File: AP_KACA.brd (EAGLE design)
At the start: 47 x 29 mm, 50 parts, among them IC1 MCP1252-33X50, J1 FTDI_DEVICE, M1 WIRELESS-NRF24L01, Q1 BSS123, Q2 BSS123, Q3 BSS123, Q4 BSS123, U1 ATMEGA328P_TQFP, U3 GY-521MPU6050, Y1 8MHz

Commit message: Airwires gone
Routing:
- net MOTOR_3: track 1.77 -> 41.8 mm, vias 1 -> 2
- net AGND: track 7.90 -> 47.0 mm, vias 1 -> 4
- net V_READER: track 2.09 -> 22.8 mm, vias 0 -> 3
- net MGND: track 0.00 -> 20.3 mm, vias 0 -> 1
- net SDA: track 0.00 -> 17.3 mm, vias 0 -> 2
- net DGND: track 52.4 -> 56.3 mm
- net GND: track 0.00 -> 1.32 mm
- net N$9: track 4.49 -> 5.57 mm

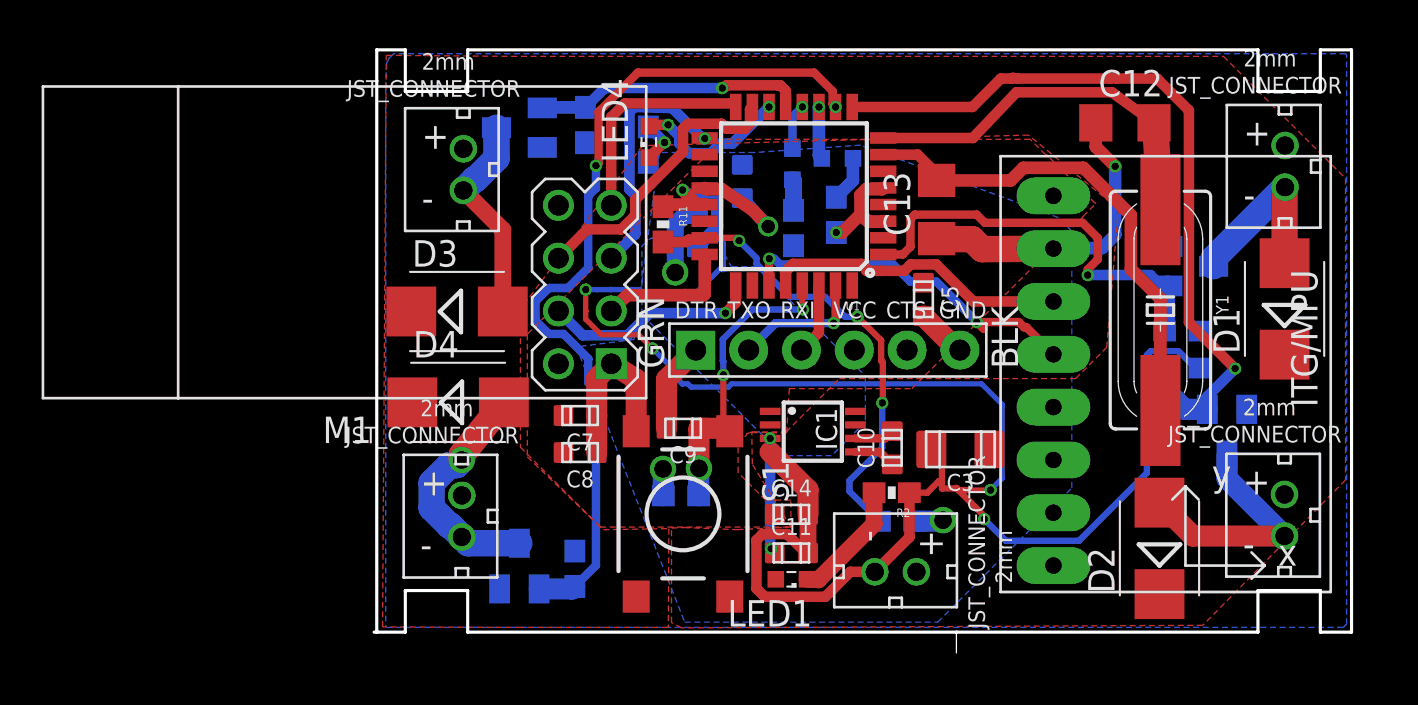
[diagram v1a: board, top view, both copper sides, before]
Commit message: finished first draft of board
got rid of all the drc errors
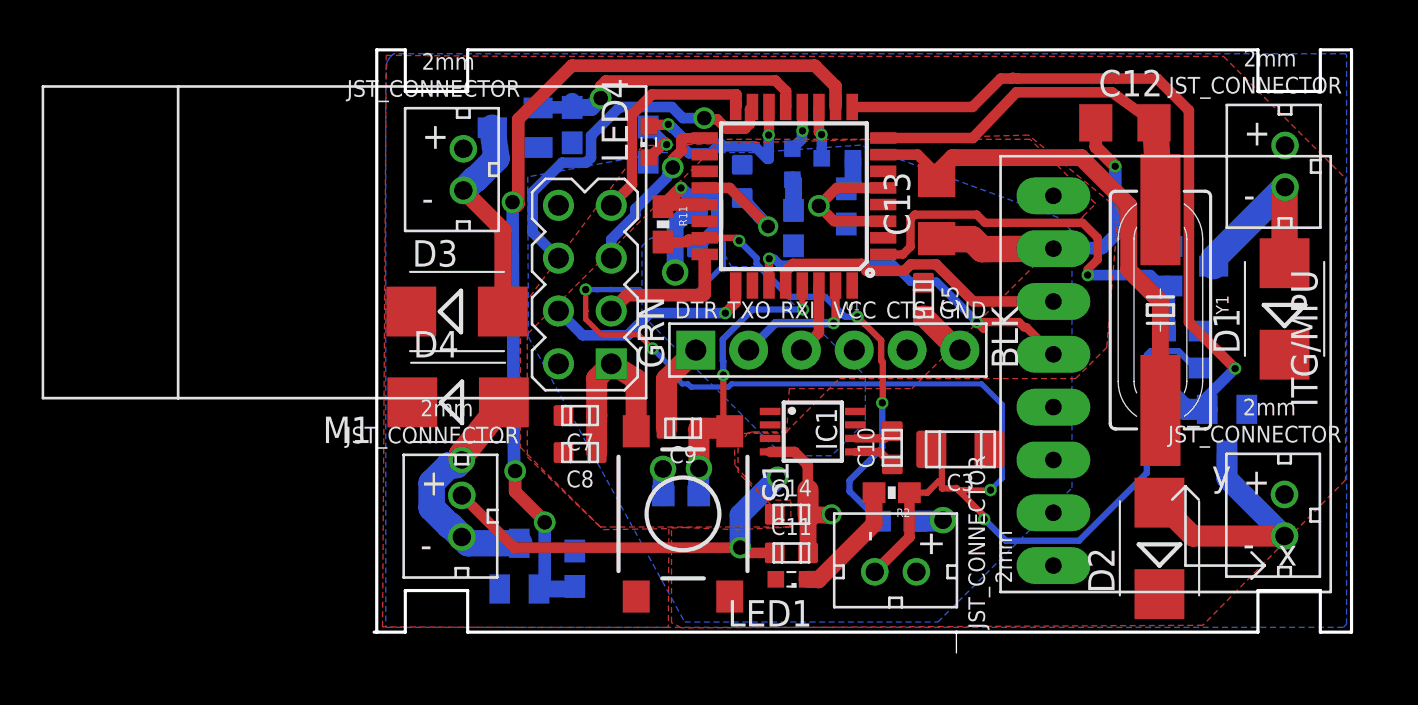
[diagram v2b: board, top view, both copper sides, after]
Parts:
- moved R5 0.63 mm to (9.53, 24.4)
- moved R7 0.63 mm to (22.7, 20.5)
- moved Q3 0.20 mm to (6.78, 24.3)
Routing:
- net 3.7V: track 7.29 -> 22.0 mm
- net DGND: track 56.3 -> 48.4 mm, vias 2 -> 3
- net MOSI: track 14.0 -> 17.9 mm, vias 0 -> 1
- net SCK: track 12.0 -> 8.25 mm
- net LED_3: track 7.51 -> 9.65 mm
- net MOTOR_3: track 41.8 -> 43.3 mm, vias 2 -> 3
- net MOTOR_4: track 13.0 -> 14.2 mm
- net N$16: track 2.20 -> 1.59 mm

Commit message: started new pcb design ver 2
ver 2 of quadcopter pcb
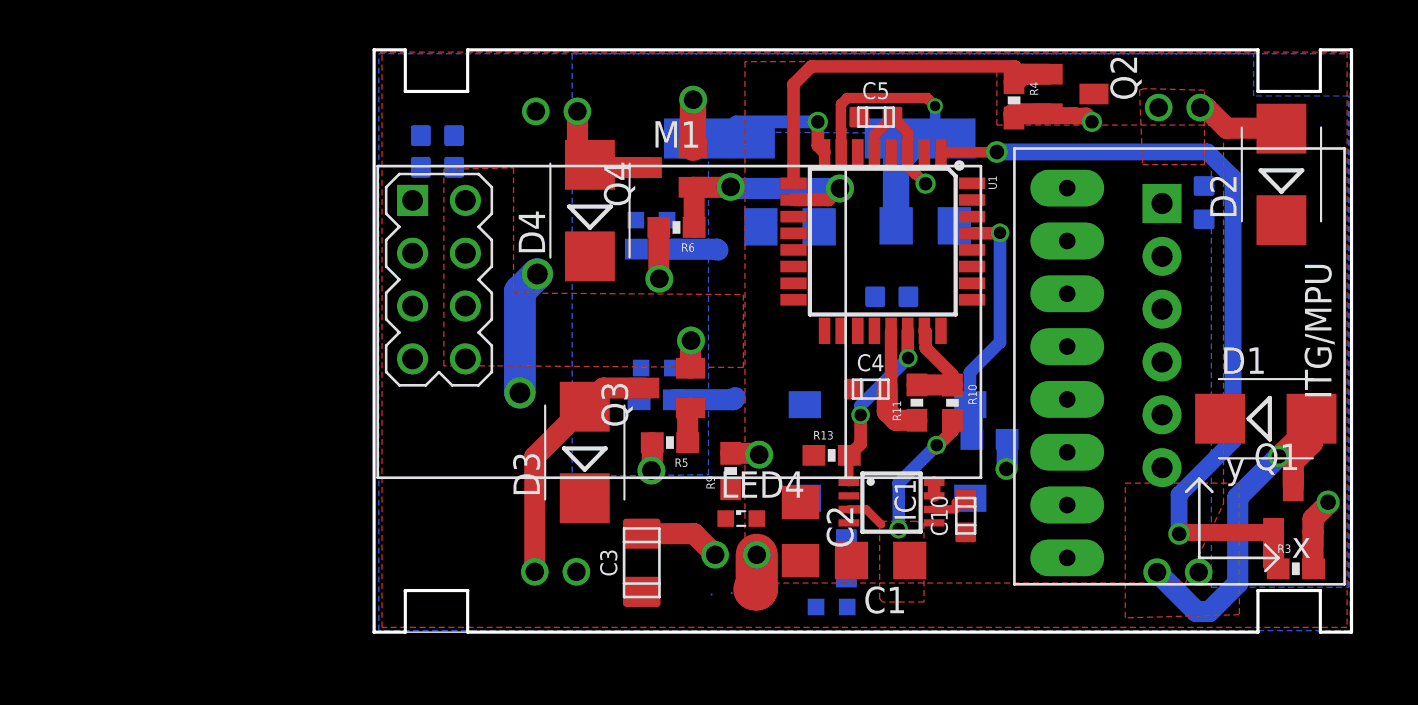
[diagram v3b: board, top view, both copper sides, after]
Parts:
- removed C11, C14: 10uF, we-rcl:C0603
- added C1, C2: 10uF, resistor:C1206
- added R13: 100k, SparkFun-Resistors:0603
- moved C9 27.3 mm to (39.9, 20.7), flipped to the bottom, turned to 180 degrees
- moved Q4 20.5 mm to (14.2, 22.3), flipped to the top, turned to 90 degrees
- moved U$3 20.2 mm to (38.7, 25.2), flipped to the bottom, turned to 270 degrees
- moved JST_MOTOR_1 20.2 mm to (38.6, 2.88), flipped to the bottom, turned to 90 degrees
- moved U$4 20.0 mm to (8.78, 25.0), flipped to the bottom, turned to 270 degrees
- moved U$5 19.8 mm to (8.73, 2.90), flipped to the bottom, turned to 90 degrees
- moved D2 18.9 mm to (43.6, 22.0)
- moved LED4 18.6 mm to (17.7, 5.46), turned to 0 degrees
- moved Y1 18.3 mm to (21.4, 23.7), flipped to the bottom, turned to 180 degrees
- moved Q2 17.9 mm to (33.5, 25.9), flipped to the top, turned to 270 degrees
- moved R6 17.1 mm to (14.5, 19.5), flipped to the top, turned to 180 degrees
- moved C12 16.9 mm to (20.0, 19.5), flipped to the bottom, turned to 180 degrees
- moved M1 16.6 mm to (14.6, 14.4), turned to 0 degrees
- moved C3 16.3 mm to (12.9, 3.34), turned to 0 degrees
- moved R9 16.2 mm to (17.1, 7.75), flipped to the top, turned to 90 degrees
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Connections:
- new net PGOOD: IC1.1, R13.2, U1.22
- net 3.3V: now also C2.1, R13.1; no longer C14.2
- net 3.7V: now also C1.1; no longer C11.2
- net DGND: now also C1.2, C2.2; no longer C11.1, C14.1
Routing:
- net AGND: track 47.1 -> 5.56 mm, vias 4 -> 0
- net DGND: track 48.4 -> 16.5 mm, vias 3 -> 2
- net MOTOR_3: track 43.3 -> 11.5 mm, vias 3 -> 2
- net MOTOR_1: track 20.6 -> 39.2 mm, vias 1 -> 2
- net MOTOR_2: track 36.7 -> 18.1 mm, vias 1 -> 0
- net V_READER: track 22.8 -> 4.87 mm, vias 3 -> 0
- net MOSI: track 17.9 -> 0.00 mm, vias 1 -> 0
- net SDA: track 17.3 -> 0.00 mm, vias 2 -> 0
- net SCL: track 14.8 -> 0.00 mm
- net MOTOR_4: track 14.2 -> 1.73 mm, vias 1 -> 0
- net N$7: track 18.6 -> 6.66 mm, vias 0 -> 1
- net MISO: track 10.8 -> 0.00 mm
- net N$6: track 24.3 -> 13.7 mm, vias 0 -> 1
- net CSN: track 10.5 -> 0.00 mm, vias 1 -> 0
- net LED_3: track 9.65 -> 0.00 mm, vias 2 -> 0
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- removed copper zone on layer 16, net AGND
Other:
- board size 47 x 29 mm -> 47 x 28 mm

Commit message: did more traces
just a few airwires left but they are hard to trace
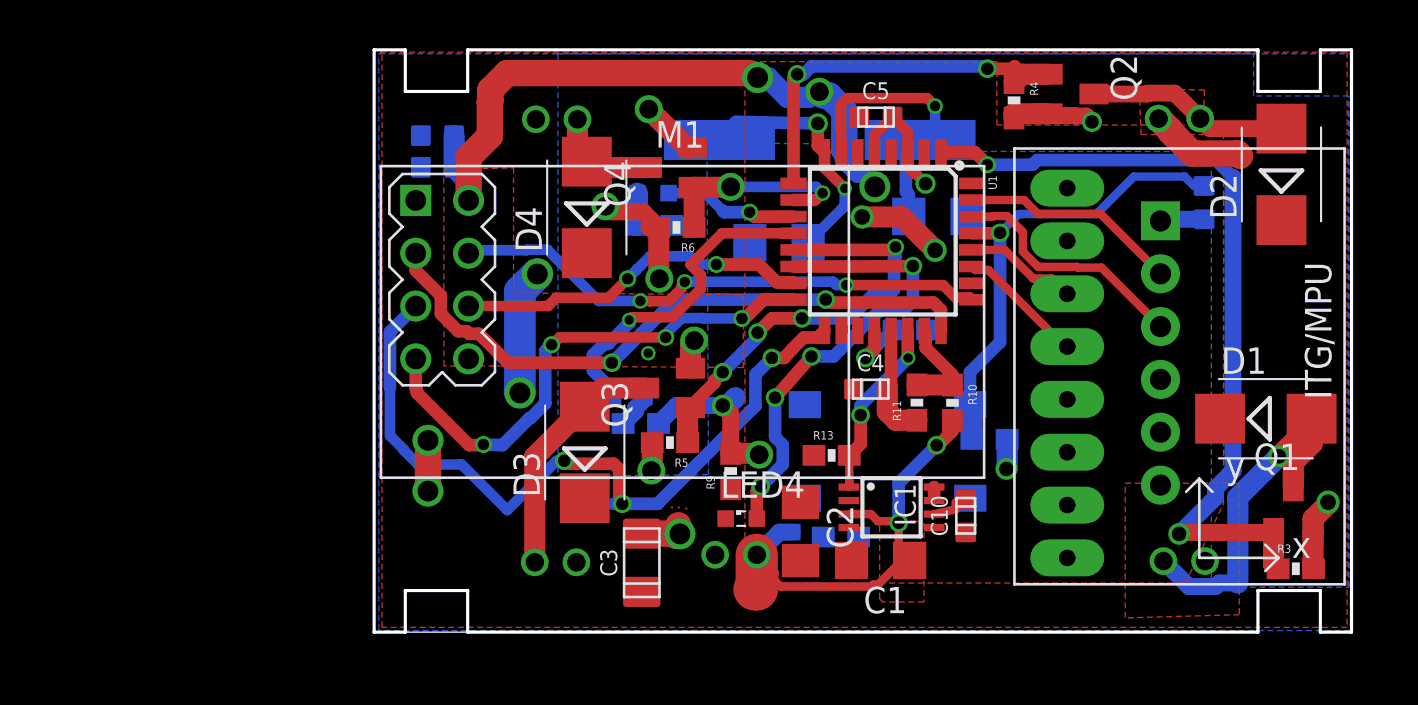
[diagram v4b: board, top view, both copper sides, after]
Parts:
- moved U$6 5.25 mm to (15.0, 5.94), flipped to the top
- moved U$8 4.84 mm to (14.7, 5.99), flipped to the top
- moved U$7 4.60 mm to (14.3, 5.99), flipped to the top
- moved LED1 3.42 mm to (20.1, 4.06), turned to 90 degrees
- moved LED3 1.94 mm to (12.2, 11.3), turned to 0 degrees
- moved C6 1.81 mm to (25.7, 14.5)
- moved R8 1.37 mm to (12.8, 10.0)
- moved LED2 1.30 mm to (13.4, 21.1)
- moved R7 1.14 mm to (13.5, 19.6)
- moved R2 1.05 mm to (22.4, 4.57), turned to 0 degrees
- moved C12 0.93 mm to (19.5, 18.7)
- moved J1 0.84 mm to (37.8, 13.4)
- moved C13 0.76 mm to (27.1, 20.0)
- moved JST_MOTOR_1 0.61 mm to (39.0, 3.42)
- moved U$3 0.53 mm to (38.7, 24.7)
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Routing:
- net SCK: track 0.00 -> 36.8 mm, vias 0 -> 3
- net 3.3V: track 1.44 -> 33.8 mm, vias 1 -> 4
- net CE: track 0.00 -> 30.9 mm, vias 0 -> 2
- net CSN: track 0.00 -> 26.1 mm, vias 0 -> 3
- net MISO: track 0.00 -> 25.6 mm, vias 0 -> 4
- net LED_3: track 0.00 -> 22.7 mm, vias 0 -> 4
- net MOTOR_4: track 1.73 -> 21.2 mm, vias 0 -> 4
- net MOSI: track 0.00 -> 17.2 mm, vias 0 -> 2
- net 3.7V: track 17.0 -> 34.1 mm
- net LED_2: track 0.00 -> 16.0 mm, vias 0 -> 1
- net RX: track 0.00 -> 11.8 mm
- net RESET: track 11.9 -> 23.1 mm
- net TX: track 0.00 -> 10.5 mm
- net LED_1: track 0.00 -> 6.46 mm, vias 0 -> 1
- net SDA: track 0.00 -> 6.17 mm
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
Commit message: fixed airwires
only 5 airwires left
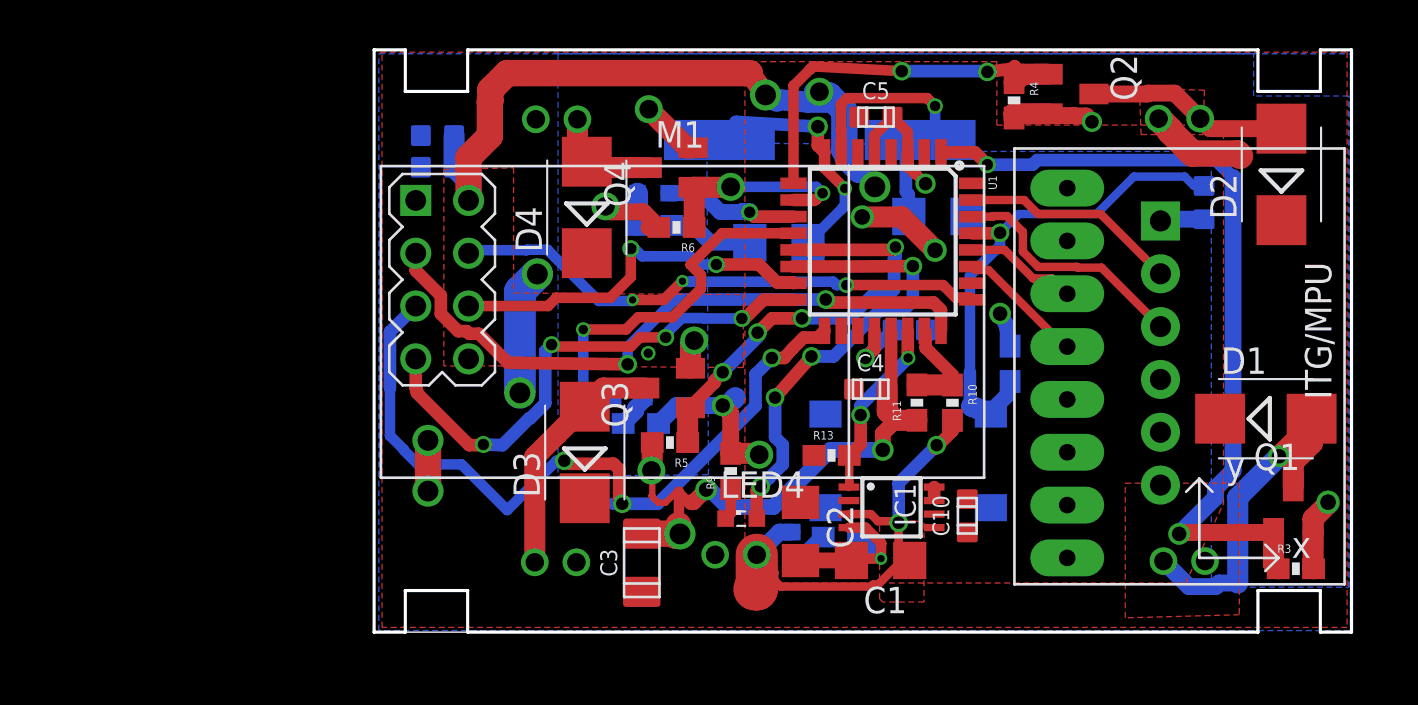
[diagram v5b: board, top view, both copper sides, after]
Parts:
- moved R1 3.76 mm to (30.6, 12.9), turned to 90 degrees
- moved S1 1.09 mm to (25.7, 8.23)
- moved U$8 0.76 mm to (14.7, 6.76)
- moved U$6 0.38 mm to (15.2, 6.25)
- moved U$7 0.38 mm to (14.0, 6.22)
- moved C10 0.08 mm to (28.5, 5.59)
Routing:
- net DGND: track 22.3 -> 36.7 mm, vias 8 -> 9
- net AGND: track 5.56 -> 18.2 mm, vias 0 -> 2
- net RESET: track 23.1 -> 25.3 mm
- net LED_2: track 16.0 -> 18.2 mm
- net 3.3V: track 33.8 -> 36.0 mm
- net N$5: track 0.00 -> 2.01 mm
- net GND: track 0.00 -> 1.65 mm
- net N$17: track 0.00 -> 1.54 mm
- net N$12: track 1.40 -> 0.00 mm
- net MOSI: track 17.2 -> 18.3 mm
- net CE: track 30.9 -> 31.5 mm
- net MGND: track 19.3 -> 19.0 mm, vias 7 -> 6

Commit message: ALMOST completed pcb
still needs the airwires for the splitter. fixed bottlenecks
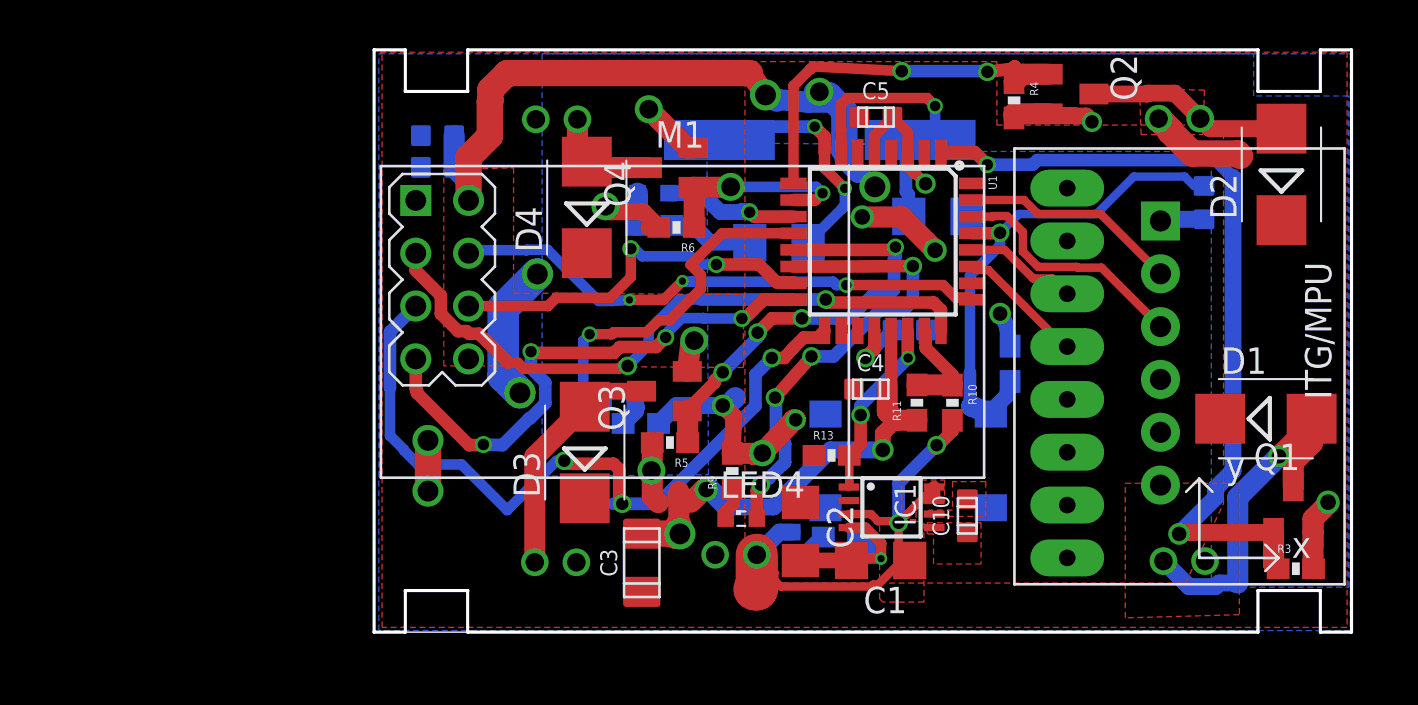
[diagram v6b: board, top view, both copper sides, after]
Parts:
- moved LED3 0.48 mm to (11.8, 11.2)
- moved Q3 0.22 mm to (14.0, 11.6)
- moved R9 0.08 mm to (17.2, 7.75)
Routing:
- net 3.7V: track 34.1 -> 37.2 mm
- net DGND: track 36.7 -> 39.2 mm, vias 9 -> 10
- net GND: track 1.65 -> 0.00 mm
- net LED_2: track 18.2 -> 17.1 mm
- net MISO: track 25.7 -> 26.6 mm
- added copper zone on layer 1, net N$11
- added copper zone on layer 1, net N$12
